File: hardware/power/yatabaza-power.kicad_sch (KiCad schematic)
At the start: 34 parts, among them CON1 POWER, P10 5V, P4 POWER, P5 HV, P6 SUPPORT, P7 SCREW, P8 SCREW, P9 12V, Q1 BC338, Q4 BC328

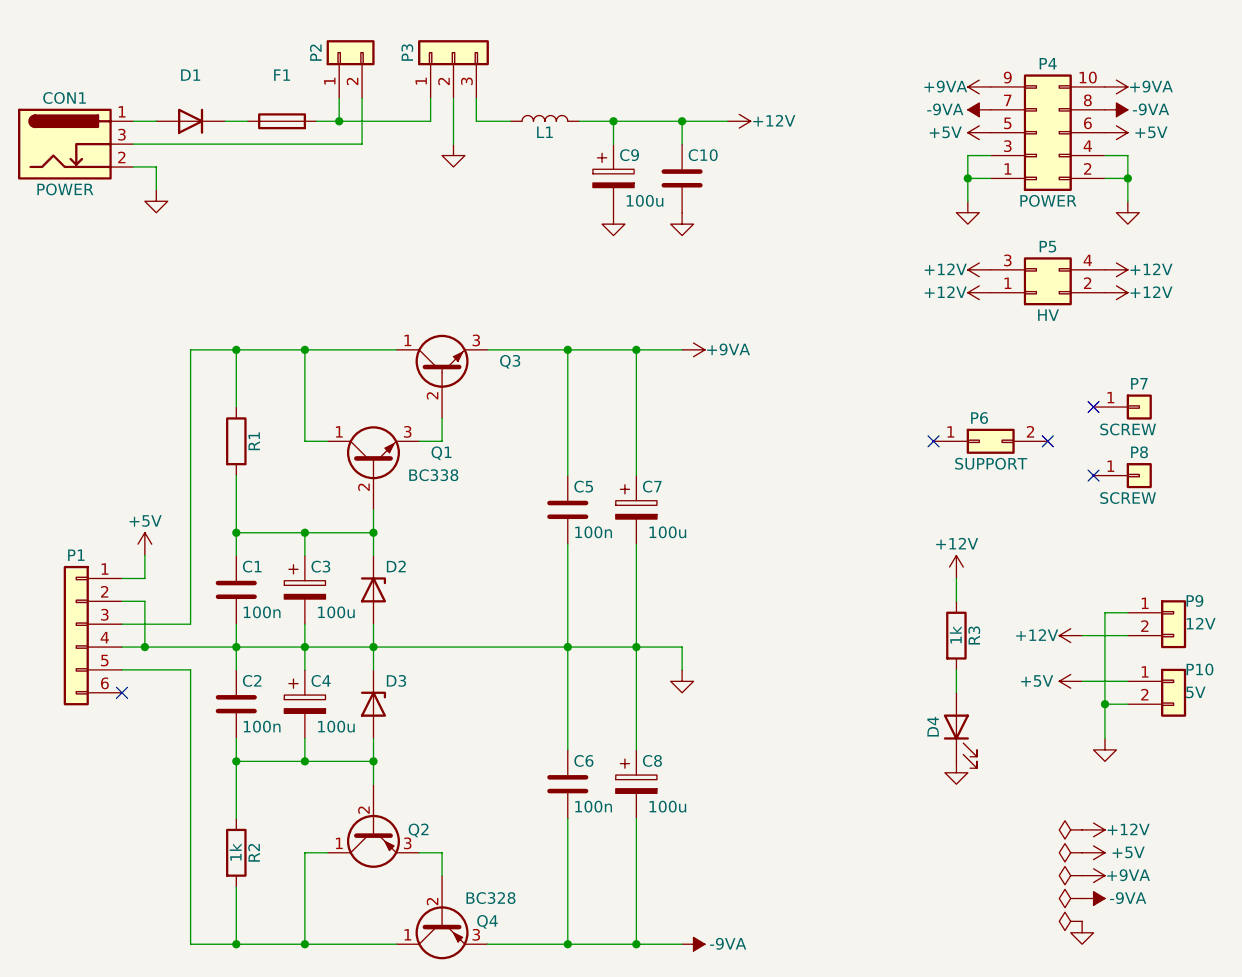
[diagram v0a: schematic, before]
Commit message: ~ Change resistors to US style.
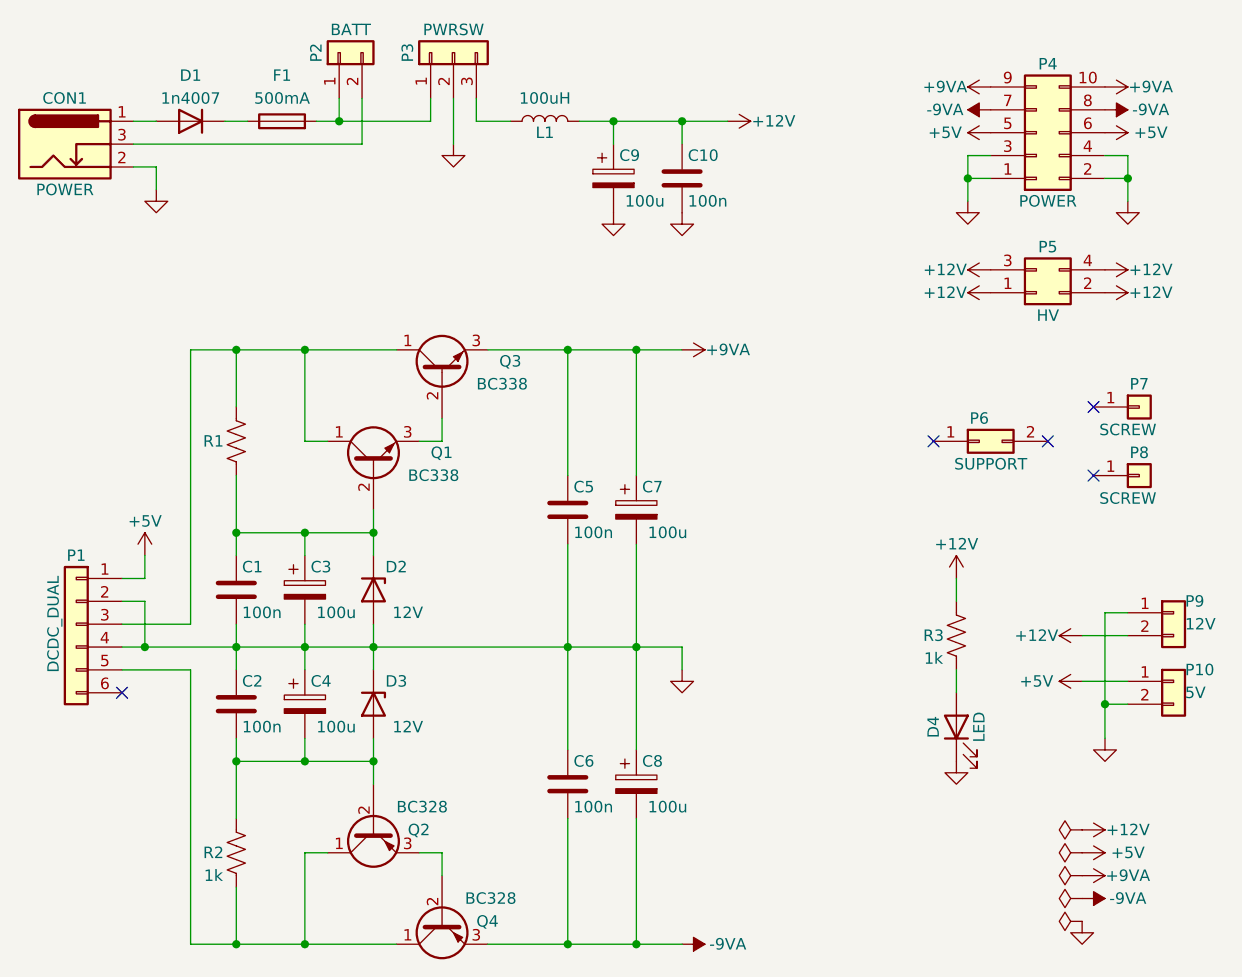
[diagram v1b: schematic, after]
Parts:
- C10: value (none) -> 100n
- D1: value (none) -> 1n4007
- D2, D3: value (none) -> 12V
- D4: value (none) -> LED
- F1: value (none) -> 500mA
- L1: value (none) -> 100uH
- P1: value (none) -> DCDC_DUAL
- P2: value (none) -> BATT
- P3: value (none) -> PWRSW
- Q2: value (none) -> BC328
- Q3: value (none) -> BC338; footprint (none) -> Package_TO_SOT_THT:TO-92
- R1: footprint Resistor_THT:R_Axial_DIN0204_L3.6mm_D1.6mm_P2.54mm_Vertical -> (none); symbol Device:R -> Device:R_US
- R2, R3: symbol Device:R -> Device:R_US
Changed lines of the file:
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@@
     (in_bom yes) (on_board yes)
     (property "Reference" "P2" (id 0) (at 59.69 26.67 0))
-    (property "Value" "" (id 1) (at 63.5 24.13 90))
+    (property "Value" "BATT" (id 1) (at 63.5 24.13 90))
     (property "Footprint" "Connector_PinHeader_2.54mm:PinHeader_1x02_P2.54mm_Vertical" (id 2) (at 62.23 26.67 0)
       (effects (font (size 1.27 1.27)) hide)
@@
     (in_bom yes) (on_board yes)
     (property "Reference" "F1" (id 0) (at 55.88 29.21 90))
-    (property "Value" "" (id 1) (at 55.88 31.75 90))
+    (property "Value" "500mA" (id 1) (at 55.88 31.75 90))
     (property "Footprint" "Fuse:Fuseholder_Cylinder-5x20mm_Schurter_0031_8201_Horizontal_Open" (id 2) (at 55.88 36.068 90)
       (effects (font (size 1.27 1.27)) hide)
@@
     (in_bom yes) (on_board yes)
     (property "Reference" "L1" (id 0) (at 85.09 35.56 90))
-    (property "Value" "" (id 1) (at 85.09 31.75 90))
+    (property "Value" "100uH" (id 1) (at 85.09 31.75 90))
     (property "Footprint" "Inductor_THT:L_Toroid_Horizontal_D3.2mm_P6.40mm_Diameter3-5mm_Amidon-T12" (id 2) (at 85.09 34.29 0)
       (effects (font (size 1.27 1.27)) hide)
@@
       (effects (font (size 1.27 1.27)) (justify left))
     )
-    (property "Value" "" (id 1) (at 100.965 43.18 0)
+    (property "Value" "100n" (id 1) (at 100.965 43.18 0)
       (effects (font (size 1.27 1.27)) (justify left))
     )
@@
     (pin "1")
   )
-  (symbol (lib_id "Device:R") (at 130.81 91.44 0) (unit 1)
-    (in_bom yes) (on_board yes)
-    (property "Reference" "R3" (id 0) (at 132.842 91.44 90))
-    (property "Value" "1k" (id 1) (at 130.81 91.44 90))
-    (property "Footprint" "Resistor_THT:R_Axial_DIN0204_L3.6mm_D1.6mm_P2.54mm_Vertical" (id 2) (at 129.032 91.44 90)
+  (symbol (lib_id "Device:R_US") (at 130.81 91.44 0) (unit 1)
+    (in_bom yes) (on_board yes)
+    (property "Reference" "R3" (id 0) (at 128.27 91.44 0))
+    (property "Value" "1k" (id 1) (at 128.27 93.98 0))
+    (property "Footprint" "Resistor_THT:R_Axial_DIN0204_L3.6mm_D1.6mm_P2.54mm_Vertical" (id 2) (at 131.826 91.694 90)
       (effects (font (size 1.27 1.27)) hide)
     )
@@
     (in_bom yes) (on_board yes)
     (property "Reference" "P1" (id 0) (at 33.02 82.55 0))
-    (property "Value" "" (id 1) (at 30.48 90.17 90))
+    (property "Value" "DCDC_DUAL" (id 1) (at 30.48 90.17 90))
     (property "Footprint" "Connector_PinHeader_2.54mm:PinHeader_1x06_P2.54mm_Vertical" (id 2) (at 33.02 90.17 0)
       (effects (font (size 1.27 1.27)) hide)
@@
       (effects (font (size 1.27 1.27)) (justify right))
     )
-    (property "Value" "" (id 1) (at 77.47 63.5 90)
+    (property "Value" "BC338" (id 1) (at 77.47 63.5 90)
       (effects (font (size 1.27 1.27)) (justify right))
     )
-    (property "Footprint" "" (id 2) (at 75.565 57.15 0)
+    (property "Footprint" "Package_TO_SOT_THT:TO-92" (id 2) (at 75.565 57.15 0)
       (effects (font (size 1.27 1.27) italic) (justify left) hide)
     )
@@
     (pin "3")
   )
-  (symbol (lib_id "Device:R") (at 50.8 69.85 0) (unit 1)
-    (in_bom yes) (on_board yes)
-    (property "Reference" "R1" (id 0) (at 52.832 69.85 90))
-    (property "Value" "" (id 1) (at 50.8 69.85 90))
-    (property "Footprint" "Resistor_THT:R_Axial_DIN0204_L3.6mm_D1.6mm_P2.54mm_Vertical" (id 2) (at 49.022 69.85 90)
+  (symbol (lib_id "Device:R_US") (at 50.8 69.85 0) (unit 1)
+    (in_bom yes) (on_board yes)
+    (property "Reference" "R1" (id 0) (at 48.26 69.85 0))
+    (property "Value" "" (id 1) (at 48.26 72.39 0))
+    (property "Footprint" "" (id 2) (at 51.816 70.104 90)
       (effects (font (size 1.27 1.27)) hide)
     )
@@
     (in_bom yes) (on_board yes)
     (property "Reference" "D2" (id 0) (at 68.58 83.82 90))
-    (property "Value" "" (id 1) (at 69.85 88.9 90))
+    (property "Value" "12V" (id 1) (at 69.85 88.9 90))
     (property "Footprint" "Diode_THT:D_DO-35_SOD27_P7.62mm_Horizontal" (id 2) (at 66.04 86.36 0)
       (effects (font (size 1.27 1.27)) hide)
@@
     (in_bom yes) (on_board yes)
     (property "Reference" "D3" (id 0) (at 68.58 96.52 90))
-    (property "Value" "" (id 1) (at 69.85 101.6 90))
+    (property "Value" "12V" (id 1) (at 69.85 101.6 90))
     (property "Footprint" "Diode_THT:D_DO-35_SOD27_P7.62mm_Horizontal" (id 2) (at 66.04 99.06 0)
       (effects (font (size 1.27 1.27)) hide)
@@
       (effects (font (size 1.27 1.27)) (justify right))
     )
-    (property "Value" "" (id 1) (at 68.58 110.49 90)
+    (property "Value" "BC328" (id 1) (at 68.58 110.49 90)
       (effects (font (size 1.27 1.27)) (justify right))
     )
@@
     (pin "3")
   )
-  (symbol (lib_id "Device:R") (at 50.8 115.57 0) (unit 1)
-    (in_bom yes) (on_board yes)
-    (property "Reference" "R2" (id 0) (at 52.832 115.57 90))
-    (property "Value" "1k" (id 1) (at 50.8 115.57 90))
-    (property "Footprint" "Resistor_THT:R_Axial_DIN0204_L3.6mm_D1.6mm_P2.54mm_Vertical" (id 2) (at 49.022 115.57 90)
+  (symbol (lib_id "Device:R_US") (at 50.8 115.57 0) (unit 1)
+    (in_bom yes) (on_board yes)
+    (property "Reference" "R2" (id 0) (at 48.26 115.57 0))
+    (property "Value" "1k" (id 1) (at 48.26 118.11 0))
+    (property "Footprint" "Resistor_THT:R_Axial_DIN0204_L3.6mm_D1.6mm_P2.54mm_Vertical" (id 2) (at 51.816 115.824 90)
       (effects (font (size 1.27 1.27)) hide)
     )
@@
     (in_bom yes) (on_board yes)
     (property "Reference" "P3" (id 0) (at 69.85 26.67 0))
-    (property "Value" "" (id 1) (at 74.93 24.13 90))
+    (property "Value" "PWRSW" (id 1) (at 74.93 24.13 90))
     (property "Footprint" "Connector_PinHeader_2.54mm:PinHeader_1x03_P2.54mm_Vertical" (id 2) (at 74.93 26.67 0)
       (effects (font (size 1.27 1.27)) hide)
@@
     (in_bom yes) (on_board yes)
     (property "Reference" "D1" (id 0) (at 45.72 29.21 0))
-    (property "Value" "" (id 1) (at 45.72 31.75 0))
+    (property "Value" "1n4007" (id 1) (at 45.72 31.75 0))
     (property "Footprint" "Diode_THT:D_DO-41_SOD81_P3.81mm_Vertical_KathodeUp" (id 2) (at 45.72 34.29 0)
       (effects (font (size 1.27 1.27)) hide)
@@
     (in_bom yes) (on_board yes)
     (property "Reference" "D4" (id 0) (at 128.27 101.6 0))
-    (property "Value" "" (id 1) (at 133.35 101.6 0))
+    (property "Value" "LED" (id 1) (at 133.35 101.6 0))
     (property "Footprint" "LED_THT:LED_D3.0mm" (id 2) (at 130.81 101.6 0)
       (effects (font (size 1.27 1.27)) hide)
